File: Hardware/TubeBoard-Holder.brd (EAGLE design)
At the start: 63.5 x 67 mm, 24 parts, among them T1 MPSA42, T2 MPSA42

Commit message: added ARM chip to driver boards to PWM tubes
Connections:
- net DRIVE_HI renamed PWM2
- net DRIVE_LO renamed PWM0
- net DRIVE_MED renamed PWM1
- net N$7 renamed PWM3
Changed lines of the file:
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@@
 <wire x1="59.69" y1="48.26" x2="59.69" y2="52.07" width="0.2032" layer="1"/>
 </signal>
-<signal name="N$7">
-<contactref element="SV1" pad="4"/>
-</signal>
-<signal name="DRIVE_LO">
+<signal name="PWM0">
 <contactref element="SV1" pad="7"/>
 </signal>
-<signal name="DRIVE_MED">
+<signal name="PWM1">
 <contactref element="SV1" pad="5"/>
 </signal>
-<signal name="DRIVE_HI">
+<signal name="PWM2">
 <contactref element="SV1" pad="3"/>
 </signal>
@@
 <wire x1="59.69" y1="24.55" x2="59.69" y2="22.07" width="0.2032" layer="1"/>
 </signal>
+<signal name="PWM3">
+<contactref element="SV1" pad="4"/>
+</signal>
 </signals>

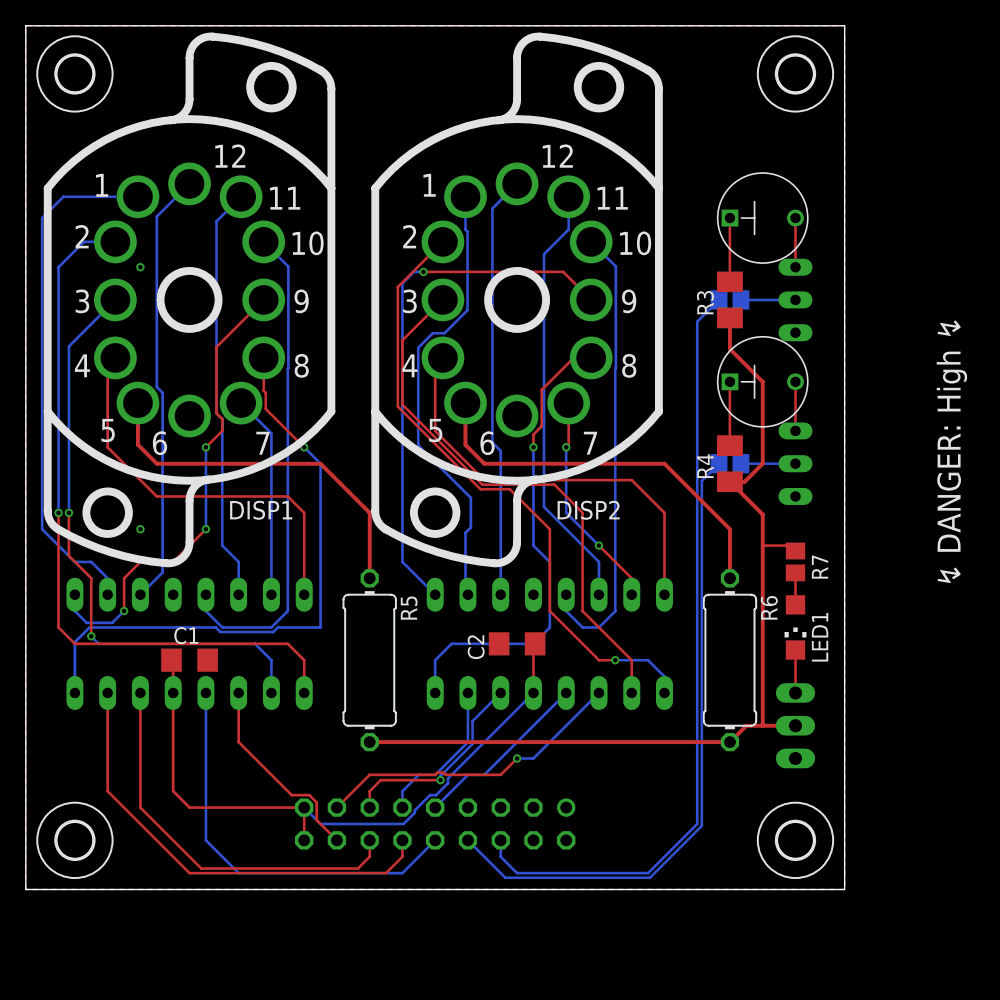
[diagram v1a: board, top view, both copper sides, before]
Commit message: added pwm drivers to tube board
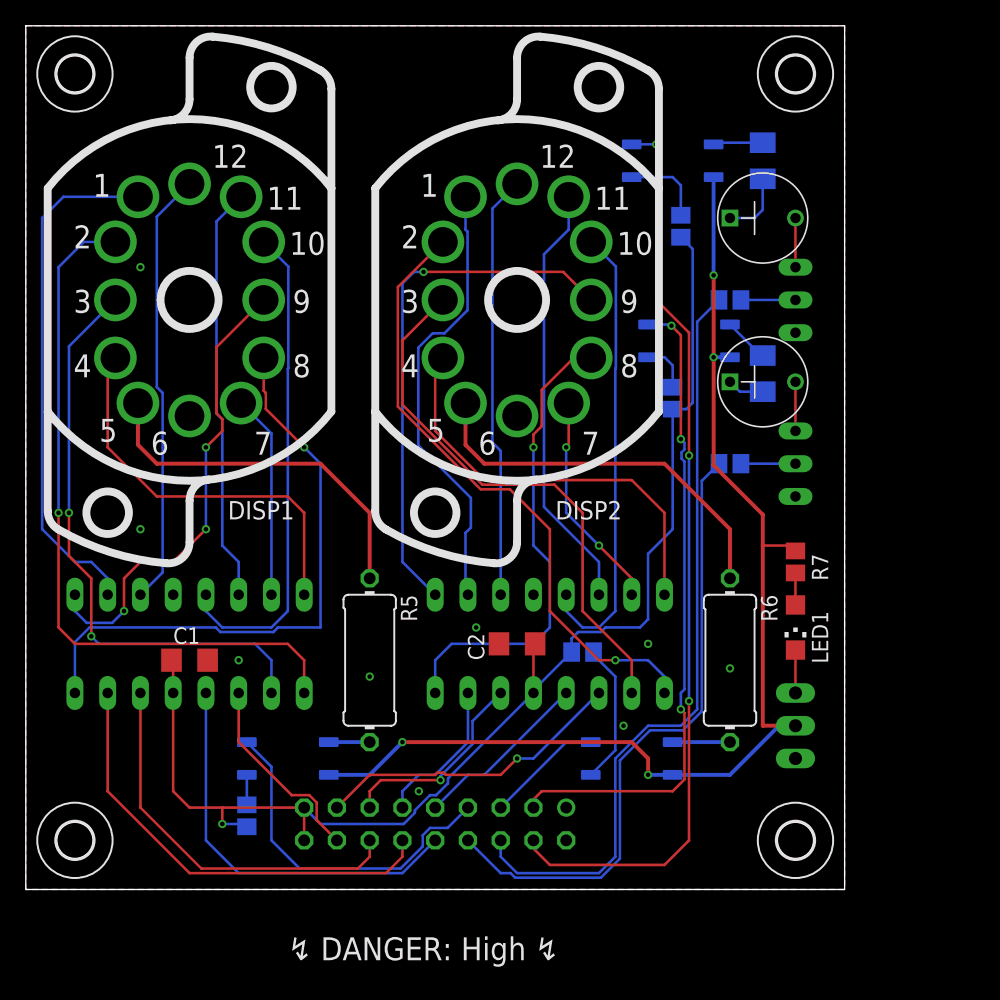
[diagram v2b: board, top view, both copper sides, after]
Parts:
- added OC1, OC2, OC3, OC4: PC-LTV352T, we-opto:MINIFLAT4
- added R10, R11, R8, R9: 330R, rcl:R2012
- R3, R4: value 174k -> 105k
- R5, R6: value 15k -> 9k1
- moved R3 11.1 mm to (57.1, 56.5), flipped to the bottom, turned to 270 degrees
- moved R4 7.43 mm to (57.1, 40.0), flipped to the bottom, turned to 270 degrees
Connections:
- new net 1_ANODE: OC1.4, R5.2
- new net 2_ANODE: OC2.4, R6.2
- new net B_ANODE: OC3.4, R4.1
- new net N$10: OC2.1, R9.2
- new net N$12: OC3.1, R10.2
- new net N$14: OC4.1, R11.2
- new net N$7: OC1.1, R8.2
- new net T_ANODE: OC4.4, R3.1
- net +5V: now also R10.1, R11.1, R8.1, R9.1
- net HV_ANODE: now also OC1.6, OC2.6, OC3.6, OC4.6; no longer R3.1, R4.1, R5.2, R6.2
- net PWM0: now also OC1.3
- net PWM1: now also OC2.3
- net PWM2: now also OC3.3
- net PWM3: now also OC4.3
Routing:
- net PWM3: track 0.00 -> 70.9 mm, vias 0 -> 3
- net PWM2: track 0.00 -> 50.9 mm, vias 0 -> 3
- net +5V: track 50.1 -> 97.5 mm, vias 0 -> 1
- net PWM0: track 0.00 -> 27.0 mm
- net HV_ANODE: track 71.7 -> 91.3 mm, vias 0 -> 4
- net N$10: track 0.00 -> 11.0 mm
- net PWM1: track 0.00 -> 9.09 mm
- net N$14: track 0.00 -> 6.40 mm
- net 2_ANODE: track 0.00 -> 4.45 mm
- net T_ANODE: track 0.00 -> 3.86 mm
- net N$12: track 0.00 -> 3.86 mm
- net B_ANODE: track 0.00 -> 3.54 mm
- net 1_ANODE: track 0.00 -> 3.18 mm
- net N$7: track 0.00 -> 2.33 mm
- net N$4: track 4.95 -> 2.86 mm
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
